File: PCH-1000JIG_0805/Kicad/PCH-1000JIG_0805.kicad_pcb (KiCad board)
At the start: 2 copper layers, 30.5 x 20.3 mm, 14 parts

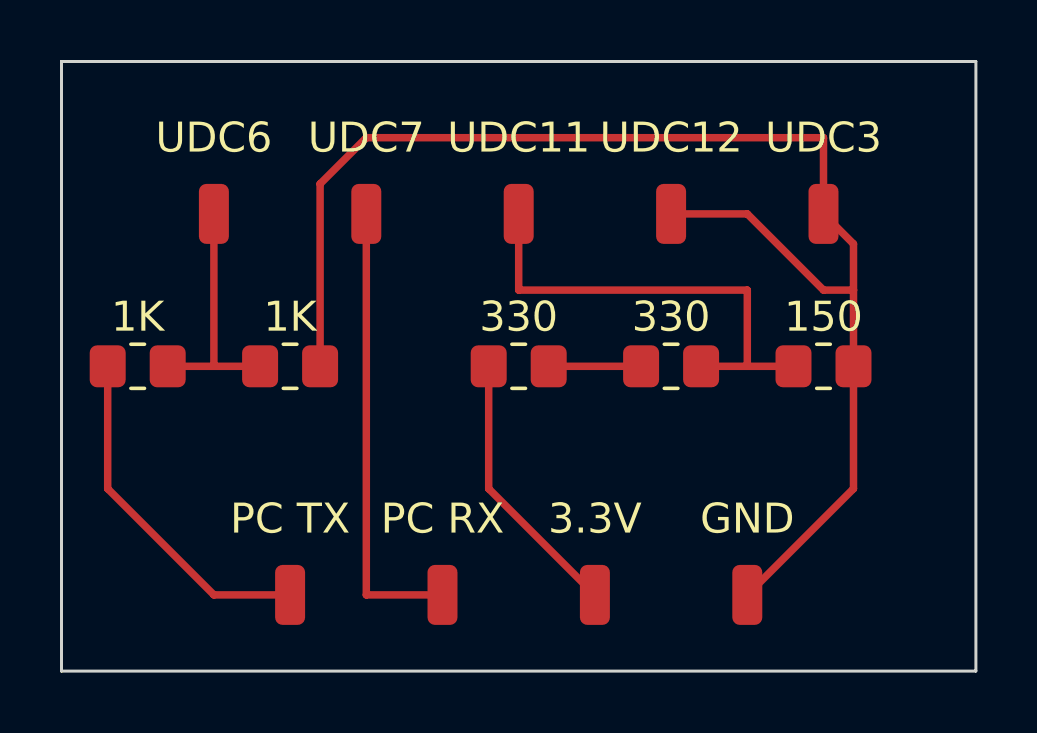
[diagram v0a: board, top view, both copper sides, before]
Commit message: The footprint is now slightly smaller.
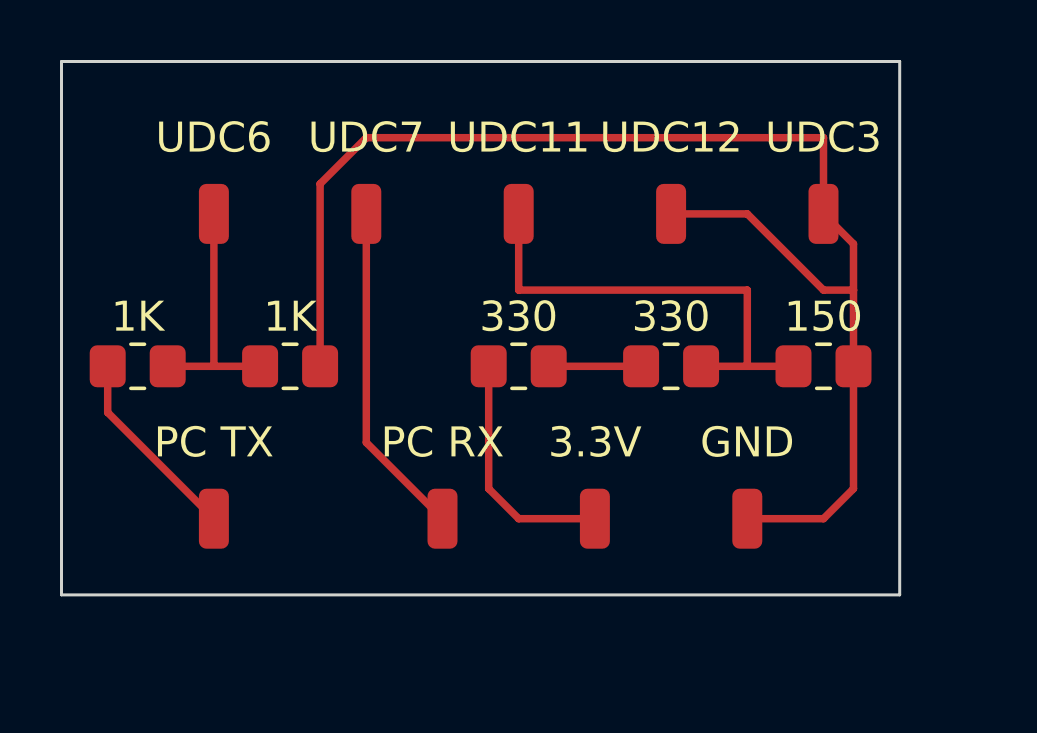
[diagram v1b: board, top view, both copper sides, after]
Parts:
- moved PC TX 3.59 mm to (40.6, 45.7)
- moved 3.3V 2.54 mm to (53.3, 45.7)
- moved GND 2.54 mm to (58.4, 45.7)
- moved PC RX 2.54 mm to (48.3, 45.7)
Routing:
- net (no net): track 110.7 -> 99.5 mm
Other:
- board size 30.5 x 20.3 mm -> 27.9 x 17.8 mm
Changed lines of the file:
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@@
   )
   (footprint "Connector_Wire:SolderWirePad_1x01_SMD_1x2mm" (layer "F.Cu")
-    (at 53.34 48.26)
+    (at 53.34 45.72)
     (descr "Wire Pad, Square, SMD Pad,  1mm x 2mm,")
     (tags "MesurementPoint Square SMDPad 1mmx2mm ")
@@
   )
   (footprint "Connector_Wire:SolderWirePad_1x01_SMD_1x2mm" (layer "F.Cu")
-    (at 48.26 48.26)
+    (at 48.26 45.72)
     (descr "Wire Pad, Square, SMD Pad,  1mm x 2mm,")
     (tags "MesurementPoint Square SMDPad 1mmx2mm ")
@@
   )
   (footprint "Connector_Wire:SolderWirePad_1x01_SMD_1x2mm" (layer "F.Cu")
-    (at 58.42 48.26)
+    (at 58.42 45.72)
     (descr "Wire Pad, Square, SMD Pad,  1mm x 2mm,")
     (tags "MesurementPoint Square SMDPad 1mmx2mm ")
@@
   )
   (footprint "Connector_Wire:SolderWirePad_1x01_SMD_1x2mm" (layer "F.Cu")
-    (at 43.18 48.26)
+    (at 40.64 45.72)
     (descr "Wire Pad, Square, SMD Pad,  1mm x 2mm,")
     (tags "MesurementPoint Square SMDPad 1mmx2mm ")
@@
     (pad "1" smd roundrect (at 0 0) (size 1 2) (layers "F.Cu" "F.Paste" "F.Mask") (roundrect_rratio 0.25))
   )
-  (gr_rect (start 35.56 30.48) (end 66.04 50.8)
+  (gr_rect (start 35.56 30.48) (end 63.5 48.26)
     (stroke (width 0.1) (type default)) (fill none) (layer "Edge.Cuts"))
   (gr_text "PCH-1000 JIG PCB REV 2.0\nBy Mathieulh" (at 38.1 38.1) (layer "B.SilkS")
     (effects (font (size 1 1) (thickness 0.2) bold) (justify left bottom))
   )
-  (segment (start 43.18 48.26) (end 40.64 48.26) (width 0.25) (layer "F.Cu") (net 0))
   (segment (start 61.96 38.1) (end 61.96 40.64) (width 0.25) (layer "F.Cu") (net 0))
   (segment (start 44.18 40.64) (end 44.18 34.56) (width 0.25) (layer "F.Cu") (net 0))
-  (segment (start 53.34 48.26) (end 49.8 44.72) (width 0.25) (layer "F.Cu") (net 0))
-  (segment (start 37.1 44.72) (end 37.1 40.64) (width 0.25) (layer "F.Cu") (net 0))
+  (segment (start 37.1 42.18) (end 40.64 45.72) (width 0.25) (layer "F.Cu") (net 0))
+  (segment (start 61.96 44.72) (end 60.96 45.72) (width 0.25) (layer "F.Cu") (net 0))
   (segment (start 58.42 38.1) (end 50.8 38.1) (width 0.25) (layer "F.Cu") (net 0))
   (segment (start 49.8 44.72) (end 49.8 40.64) (width 0.25) (layer "F.Cu") (net 0))
-  (segment (start 40.64 48.26) (end 37.1 44.72) (width 0.25) (layer "F.Cu") (net 0))
   (segment (start 61.96 36.56) (end 61.96 38.1) (width 0.25) (layer "F.Cu") (net 0))
+  (segment (start 37.1 42.18) (end 37.1 40.64) (width 0.25) (layer "F.Cu") (net 0))
   (segment (start 60.96 35.56) (end 61.96 36.56) (width 0.25) (layer "F.Cu") (net 0))
   (segment (start 51.8 40.64) (end 54.88 40.64) (width 0.25) (layer "F.Cu") (net 0))
+  (segment (start 49.8 44.72) (end 50.8 45.72) (width 0.25) (layer "F.Cu") (net 0))
+  (segment (start 50.8 45.72) (end 53.34 45.72) (width 0.25) (layer "F.Cu") (net 0))
   (segment (start 58.42 35.56) (end 60.96 38.1) (width 0.25) (layer "F.Cu") (net 0))
-  (segment (start 58.42 48.26) (end 61.96 44.72) (width 0.25) (layer "F.Cu") (net 0))
   (segment (start 50.8 38.1) (end 50.8 35.56) (width 0.25) (layer "F.Cu") (net 0))
   (segment (start 58.42 40.64) (end 59.96 40.64) (width 0.25) (layer "F.Cu") (net 0))
   (segment (start 44.18 34.56) (end 45.72 33.02) (width 0.25) (layer "F.Cu") (net 0))
+  (segment (start 45.72 43.18) (end 48.26 45.72) (width 0.25) (layer "F.Cu") (net 0))
   (segment (start 60.96 38.1) (end 61.96 38.1) (width 0.25) (layer "F.Cu") (net 0))
   (segment (start 40.64 35.56) (end 40.64 40.64) (width 0.25) (layer "F.Cu") (net 0))
+  (segment (start 45.72 35.56) (end 45.72 43.18) (width 0.25) (layer "F.Cu") (net 0))
   (segment (start 58.42 40.64) (end 58.42 38.1) (width 0.25) (layer "F.Cu") (net 0))
   (segment (start 39.1 40.64) (end 42.18 40.64) (width 0.25) (layer "F.Cu") (net 0))
   (segment (start 56.88 40.64) (end 58.42 40.64) (width 0.25) (layer "F.Cu") (net 0))
   (segment (start 55.88 35.56) (end 58.42 35.56) (width 0.25) (layer "F.Cu") (net 0))
+  (segment (start 60.96 45.72) (end 58.42 45.72) (width 0.25) (layer "F.Cu") (net 0))
   (segment (start 60.96 33.02) (end 60.96 35.56) (width 0.25) (layer "F.Cu") (net 0))
-  (segment (start 45.72 48.26) (end 48.26 48.26) (width 0.25) (layer "F.Cu") (net 0))
   (segment (start 61.96 44.72) (end 61.96 40.64) (width 0.25) (layer "F.Cu") (net 0))
-  (segment (start 45.72 35.56) (end 45.72 48.26) (width 0.25) (layer "F.Cu") (net 0))
   (segment (start 45.72 33.02) (end 60.96 33.02) (width 0.25) (layer "F.Cu") (net 0))
 )
